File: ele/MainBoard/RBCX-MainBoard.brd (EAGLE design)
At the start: 100 x 100 mm, 449 parts, among them IC1 AMS1117-3.3, IC10 INA180A4, IC11 INA180A4, IC12 MPU-6050, IC13 STM32F103VCT6, IC2 DRV8833PWP, IC3 INA180A4, IC4 INA180A4, IC5 DRV8833PWP, IC6 INA180A4, IC7 INA180A4, IC8 INA180A4, IC9 INA180A4, P1 M1, P2 M2, P3 M3, P4 M4, Q1 NCE20P45Q, Q10 2N7002, Q2 NCE20P45Q, Q3 2N7002, Q4 2N7002, Q5 2N7002, Q6 2N7002, Q7 2N7002, Q8 2N7002, Q9 2N7002, X1 POWER_IN, X2 POWER_OUT, X3 52559-3092, X4 uUSB, Y1 5032/2P, Y2 3215_2P

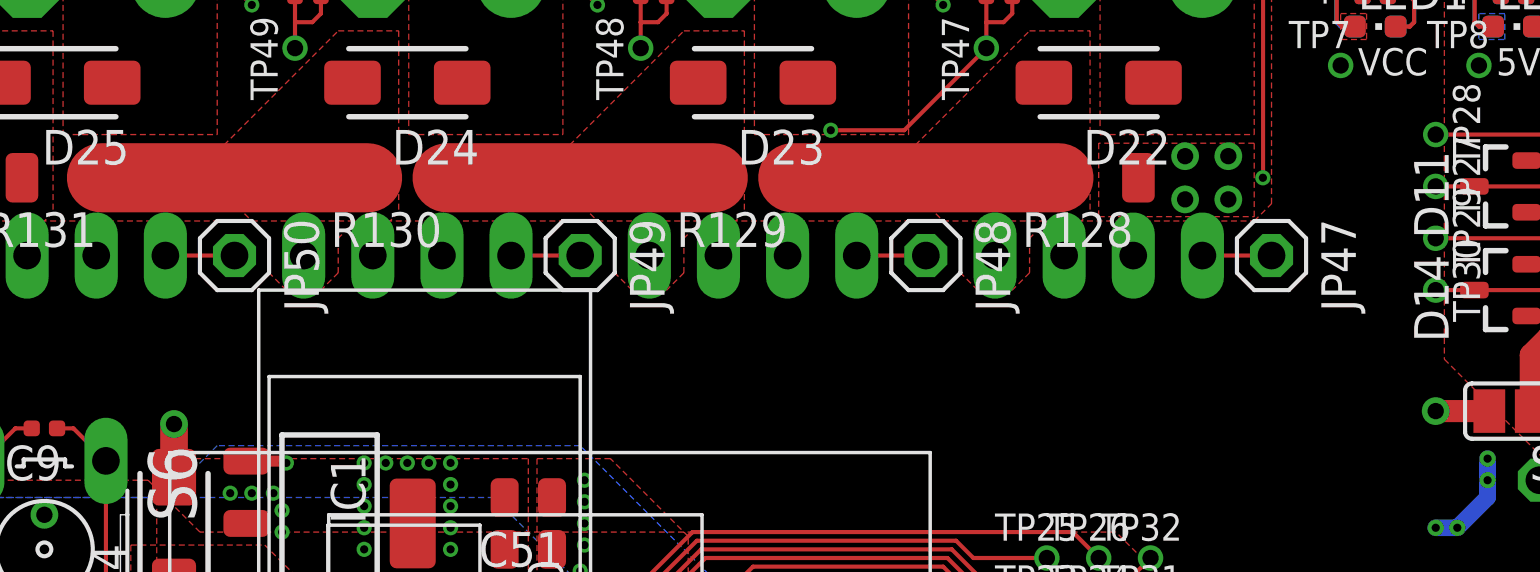
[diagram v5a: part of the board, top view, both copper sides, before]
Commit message: MainBoardBRD: Mirror servos step-down enable pin
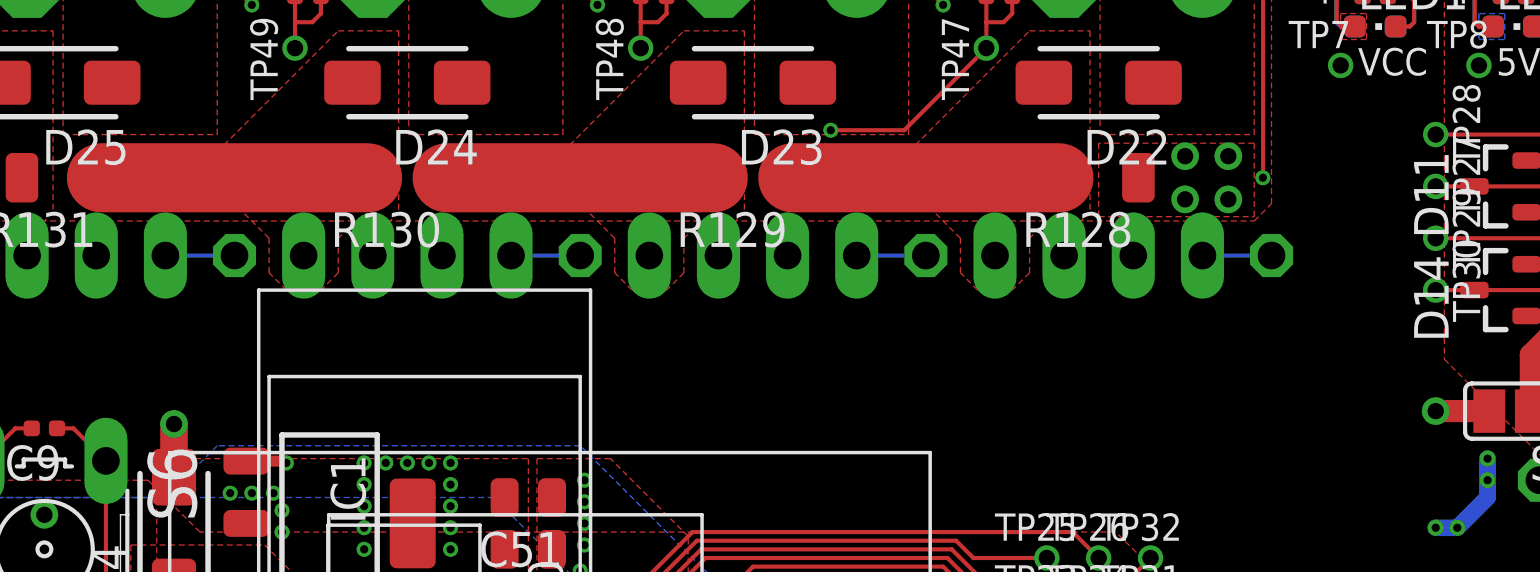
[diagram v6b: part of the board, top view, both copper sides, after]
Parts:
- flipped JP47 to the bottom
- flipped JP48 to the bottom
- flipped JP49 to the bottom
- flipped JP50 to the bottom
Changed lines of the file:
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@@
 <layers>
 <layer number="1" name="Top" color="4" fill="1" visible="no" active="yes"/>
-<layer number="2" name="Layer2-Sig" color="16" fill="1" visible="yes" active="yes"/>
+<layer number="2" name="Layer2-Sig" color="16" fill="1" visible="no" active="yes"/>
 <layer number="3" name="Route3" color="17" fill="1" visible="no" active="no"/>
 <layer number="4" name="Route4" color="18" fill="1" visible="no" active="no"/>
@@
 <attribute name="VALUE" x="57.4675" y="82.55" size="1.27" layer="28" rot="MR180"/>
 </element>
-<element name="JP47" library="pinhead" package="1X01" value="SERVO1_EN" x="69.215" y="79.375" smashed="yes" rot="R270">
-<attribute name="NAME" x="71.0438" y="80.7212" size="1.27" layer="25" ratio="10" rot="R270"/>
-<attribute name="VALUE" x="66.04" y="80.645" size="1.27" layer="27" rot="R270"/>
+<element name="JP47" library="pinhead" package="1X01" value="SERVO1_EN" x="69.215" y="79.375" smashed="yes" rot="MR270">
+<attribute name="NAME" x="67.3862" y="80.7212" size="1.27" layer="26" ratio="10" rot="MR270"/>
+<attribute name="VALUE" x="72.39" y="80.645" size="1.27" layer="28" rot="MR270"/>
 </element>
 <element name="JP51" library="pinhead" library_urn="urn:adsk.eagle:library:325" package="1X03" package3d_urn="urn:adsk.eagle:package:22458/2" value="SERVO1" x="64.135" y="98.425" smashed="yes" rot="MR0">
@@
 <attribute name="VALUE" x="44.7675" y="82.55" size="1.27" layer="28" rot="MR180"/>
 </element>
-<element name="JP48" library="pinhead" package="1X01" value="SERVO2_EN" x="56.515" y="79.375" smashed="yes" rot="R270">
-<attribute name="NAME" x="58.3438" y="80.7212" size="1.27" layer="25" ratio="10" rot="R270"/>
-<attribute name="VALUE" x="53.34" y="80.645" size="1.27" layer="27" rot="R270"/>
+<element name="JP48" library="pinhead" package="1X01" value="SERVO2_EN" x="56.515" y="79.375" smashed="yes" rot="MR270">
+<attribute name="NAME" x="54.6862" y="80.7212" size="1.27" layer="26" ratio="10" rot="MR270"/>
+<attribute name="VALUE" x="59.69" y="80.645" size="1.27" layer="28" rot="MR270"/>
 </element>
 <element name="JP52" library="pinhead" library_urn="urn:adsk.eagle:library:325" package="1X03" package3d_urn="urn:adsk.eagle:package:22458/2" value="SERVO2" x="51.435" y="98.425" smashed="yes" rot="MR0">
@@
 <attribute name="VALUE" x="32.0675" y="82.55" size="1.27" layer="28" rot="MR180"/>
 </element>
-<element name="JP49" library="pinhead" package="1X01" value="SERVO3_EN" x="43.815" y="79.375" smashed="yes" rot="R270">
-<attribute name="NAME" x="45.6438" y="80.7212" size="1.27" layer="25" ratio="10" rot="R270"/>
-<attribute name="VALUE" x="40.64" y="80.645" size="1.27" layer="27" rot="R270"/>
+<element name="JP49" library="pinhead" package="1X01" value="SERVO3_EN" x="43.815" y="79.375" smashed="yes" rot="MR270">
+<attribute name="NAME" x="41.9862" y="80.7212" size="1.27" layer="26" ratio="10" rot="MR270"/>
+<attribute name="VALUE" x="46.99" y="80.645" size="1.27" layer="28" rot="MR270"/>
 </element>
 <element name="JP53" library="pinhead" library_urn="urn:adsk.eagle:library:325" package="1X03" package3d_urn="urn:adsk.eagle:package:22458/2" value="SERVO3" x="38.735" y="98.425" smashed="yes" rot="MR0">
@@
 <attribute name="VALUE" x="19.3675" y="82.55" size="1.27" layer="28" rot="MR180"/>
 </element>
-<element name="JP50" library="pinhead" package="1X01" value="SERVO4_EN" x="31.115" y="79.375" smashed="yes" rot="R270">
-<attribute name="NAME" x="32.9438" y="80.7212" size="1.27" layer="25" ratio="10" rot="R270"/>
-<attribute name="VALUE" x="27.94" y="80.645" size="1.27" layer="27" rot="R270"/>
+<element name="JP50" library="pinhead" package="1X01" value="SERVO4_EN" x="31.115" y="79.375" smashed="yes" rot="MR270">
+<attribute name="NAME" x="29.2862" y="80.7212" size="1.27" layer="26" ratio="10" rot="MR270"/>
+<attribute name="VALUE" x="34.29" y="80.645" size="1.27" layer="28" rot="MR270"/>
 </element>
 <element name="JP54" library="pinhead" library_urn="urn:adsk.eagle:library:325" package="1X03" package3d_urn="urn:adsk.eagle:package:22458/2" value="SERVO4" x="26.035" y="98.425" smashed="yes" rot="MR0">
@@
 <contactref element="IM5" pad="EN"/>
 <contactref element="JP47" pad="1"/>
-<wire x1="66.675" y1="79.375" x2="69.215" y2="79.375" width="0.1524" layer="1"/>
+<wire x1="66.675" y1="79.375" x2="69.215" y2="79.375" width="0.1524" layer="16"/>
 </signal>
 <signal name="SERVO_1_PWR">
@@
 <contactref element="IM6" pad="EN"/>
 <contactref element="JP48" pad="1"/>
-<wire x1="53.975" y1="79.375" x2="56.515" y2="79.375" width="0.1524" layer="1"/>
+<wire x1="53.975" y1="79.375" x2="56.515" y2="79.375" width="0.1524" layer="16"/>
 </signal>
 <signal name="SERVO_2_PWR">
@@
 <contactref element="IM7" pad="EN"/>
 <contactref element="JP49" pad="1"/>
-<wire x1="41.275" y1="79.375" x2="43.815" y2="79.375" width="0.1524" layer="1"/>
+<wire x1="41.275" y1="79.375" x2="43.815" y2="79.375" width="0.1524" layer="16"/>
 </signal>
 <signal name="SERVO_3_PWR">
@@
 <contactref element="IM8" pad="EN"/>
 <contactref element="JP50" pad="1"/>
-<wire x1="28.575" y1="79.375" x2="31.115" y2="79.375" width="0.1524" layer="1"/>
+<wire x1="28.575" y1="79.375" x2="31.115" y2="79.375" width="0.1524" layer="16"/>
 </signal>
 <signal name="SERVO_4_PWR">

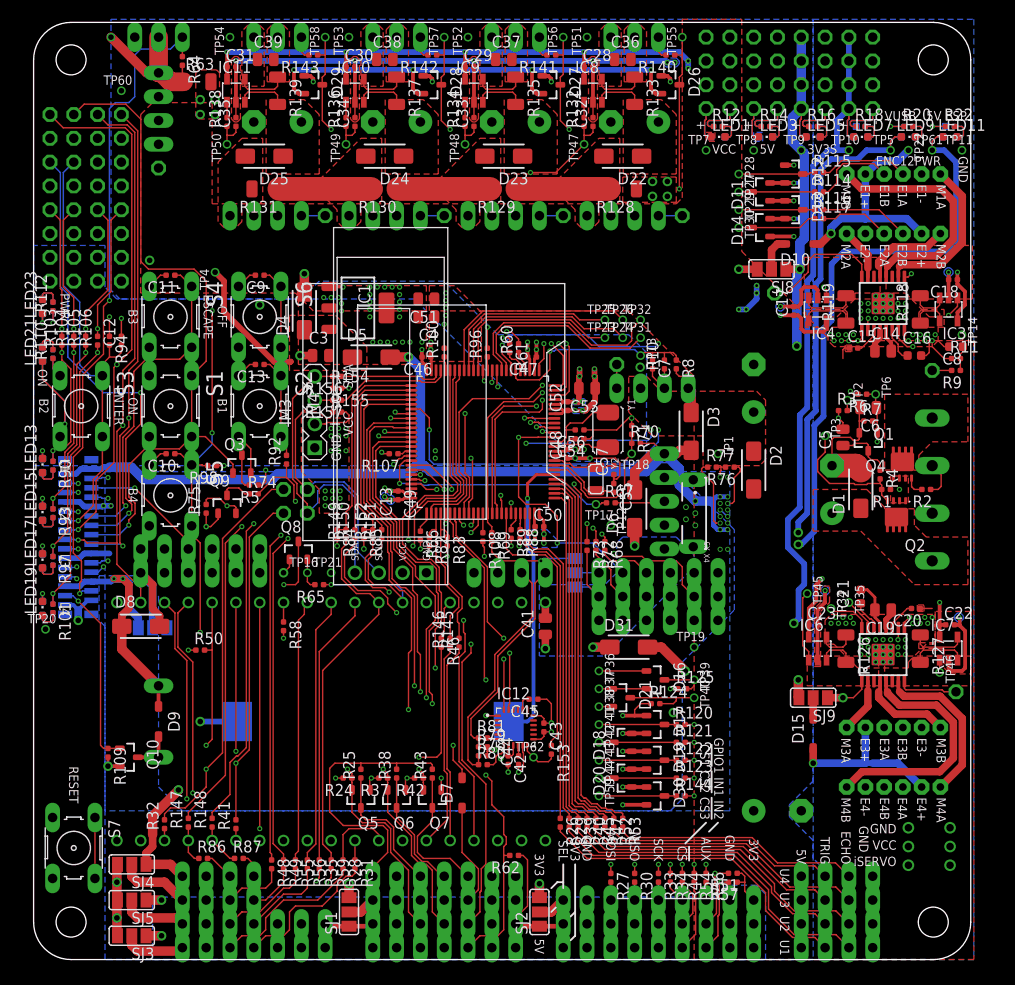
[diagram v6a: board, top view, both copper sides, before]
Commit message: MainBoardBRD: Add basic topside silkscreen
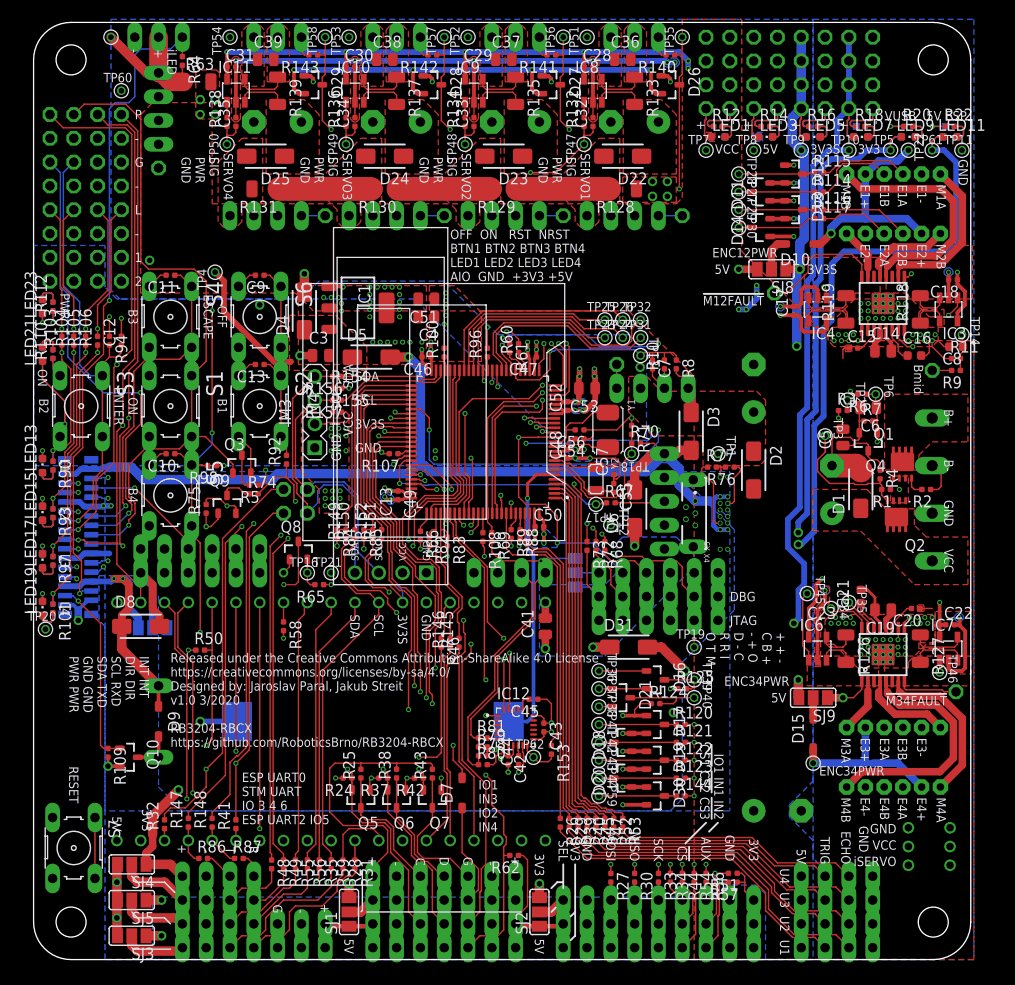
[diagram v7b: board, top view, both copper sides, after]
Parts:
- moved D25 0.16 mm to (24.8, 85.7)
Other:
- board text added: "!M12FAULT"
- board text added: "!M34FAULT"
- board text added: "+ + - C B + - + O D - C R R I O T M"
- board text added: "1"
- board text added: "2"
- board text added: "B+"
- board text added: "B-"
- board text added: "Bmid"
- board text added: "C"
- board text added: "D"
- board text added: "DBG"
- board text added: "ENC34PWR"
- board text added: "ESP UART0 STM UART IO 3 4 6 ESP UART2 IO5"
- board text added: "G"
- board text added: "INT INT DIR DIR SCL RXD SDA TXD GND GND PWR PWR"
- board text added: "IO1 IN1 IN2 !CS1! !CS2! !CS3!"
- board text added: "IO1 IN3 IO2 IN4"
- board text added: "JTAG"
- board text added: "L"
- board text added: "OFF ON RST NRST BTN1 BTN2 BTN3 BTN4 LED1 LED2 LED3 LED4 AIO GND +3V3 +5V"
- board text added: "P"
- board text added: "R"
- board text added: "Released under the Creative Commons Attribution-ShareAlike 4.0 License https://creativecommons.org/licenses/by-sa/4.0/ Designed by: Jaroslav Paral, Jakub Streit v1.0 3/2020 RB3204-RBCX https://github.com/RoboticsBrno/RB3204-RBCX"
- board text added: "SCL"
- board text added: "SDA"
- board text added: "SERVO1 SIG PWR GND"
- board text added: "SERVO2 SIG PWR GND"
- board text added: "SERVO3 SIG PWR GND"
- board text added: "SERVO4 SIG PWR GND"
- board text added: "T"
- board text added: "iLED"
- board text removed: "GPIO1 IN1 IN2 !CS1! !CS2! !CS3!"
- board text removed: "M2A"
- board text removed: "M3B"

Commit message: MainBoardBRD: Add bottom silkscreen and improve top silkscreen
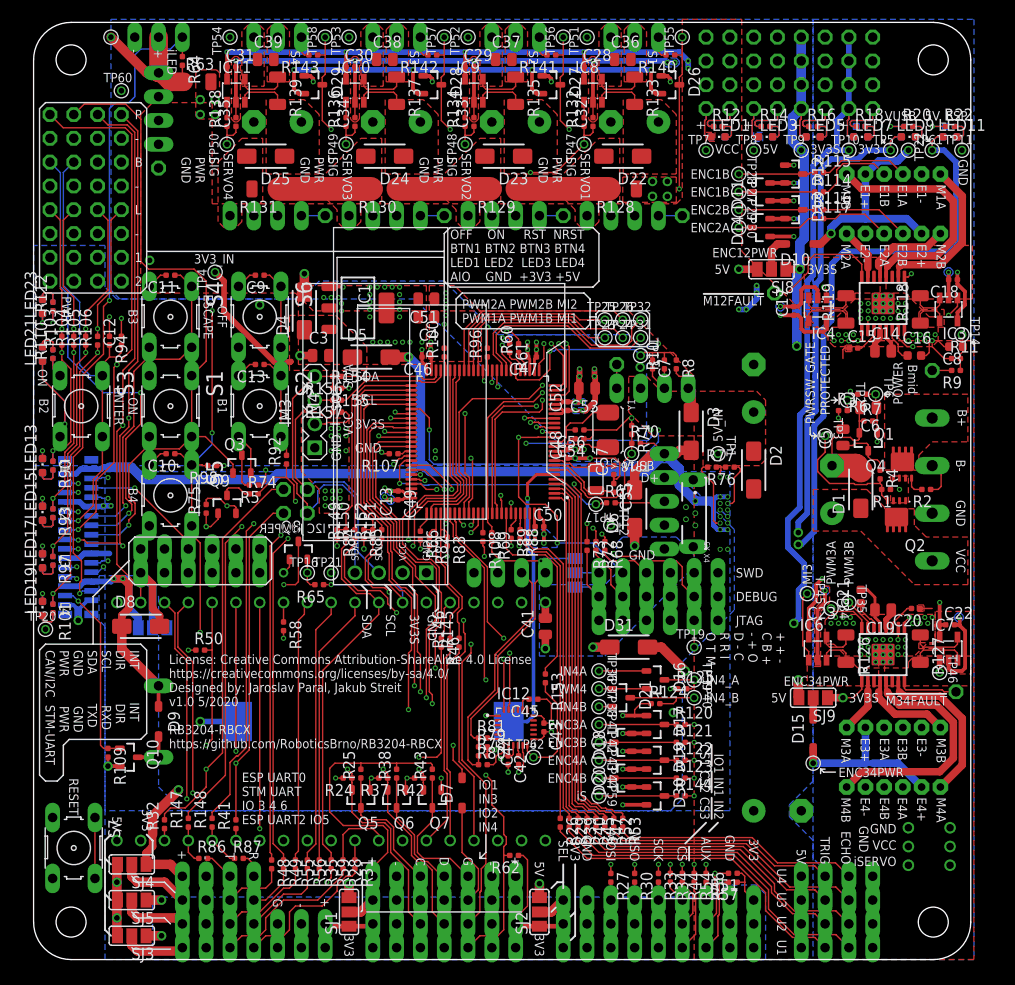
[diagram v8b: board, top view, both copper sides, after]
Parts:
- moved R153 7.65 mm to (54.6, 30.0)
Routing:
- net MPU-INT: track 4.26 -> 12.2 mm
- net MPU_INT: track 29.3 -> 22.0 mm
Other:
- board text added: "!CS1! !CS2! !CS3! IO1 IN1 IN2"
- board text added: "3V3_IN"
- board text added: "5V_ESP"
- board text added: "5V_IN"
- board text added: "B"
- board text added: "CAN/I2C STM-UART PWR PWR GND GND SDA TXD SCL RXD DIR DIR INT INT"
- board text added: "D+"
- board text added: "D-"
- board text added: "DEBUG"
- board text added: "EN"
- board text added: "ENC1B"
- board text added: "ENC2A"
- board text added: "ENC2B"
- board text added: "ENC3A"
- board text added: "ENC3B"
- board text added: "ENC4A"
- board text added: "ENC4B"
- board text added: "ESP"
- board text added: "ESP UART0 STM UART 6 4 3 IO ESP UART2 IO5"
- board text added: "I2C"
- board text added: "I2C JUMPER"
- board text added: "ID"
- board text added: "IN"
- board text added: "IN4A"
- board text added: "IN4B"
- board text added: "IN4_A"
- board text added: "IN4_B"
- board text added: "INT INT DIR DIR SCL RXD SDA TXD GND GND PWR PWR CAN/I2C STM-UART"
- board text added: "License: Creative Commons Attribution-ShareAlike 4.0 License https://creativecommons.org/licenses/by-sa/4.0/ Designed by: Jaroslav Paral, Jakub Streit v1.0 5/2020 RB3204-RBCX https://github.com/RoboticsBrno/RB3204-RBCX"
- board text added: "M2A"
- board text added: "M3B"
- board text added: "MI2 PWM2B PWM2A MI1 PWM1B PWM1A"
- board text added: "MI3"
- board text added: "NRST RST ON OFF BTN4 BTN3 BTN2 BTN1 LED4 LED3 LED2 LED1 +5V +3V3 GND AIO"
- board text added: "O T M R R I D - C - + O C B + + + -"
- board text added: "OUT"
- board text added: "POWER"
- board text added: "PROTECTED"
- board text added: "PWM2A PWM2B MI2 PWM1A PWM1B MI1"
- board text added: "PWM3A"
- board text added: "PWM3B"
- board text added: "PWM4"
- board text added: "PWRSW_GATE"
- board text added: "RB3204-RBCX v1.0 5/2020 https://github.com/ RoboticsBrno/RB3204-RBCX CC-SA 4.0"
- board text added: "S1"
- board text added: "S2"
- board text added: "S3"
- board text added: "S4"
- board text added: "SPI"
- board text added: "STM"
- board text added: "SWD"
- board text added: "UART"
- board text added: "UI BOARD CONNECTOR"
- board text added: "iS"
- board text removed: "5V ESP"
- board text removed: "DBG"
- board text removed: "INT INT DIR DIR SCL RXD SDA TXD GND GND PWR PWR"
- board text removed: "Released under the Creative Commons Attribution-ShareAlike 4.0 License https://creativecommons.org/licenses/by-sa/4.0/ Designed by: Jaroslav Paral, Jakub Streit v1.0 3/2020 RB3204-RBCX https://github.com/RoboticsBrno/RB3204-RBCX"
